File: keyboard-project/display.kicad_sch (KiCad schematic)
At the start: 0 parts

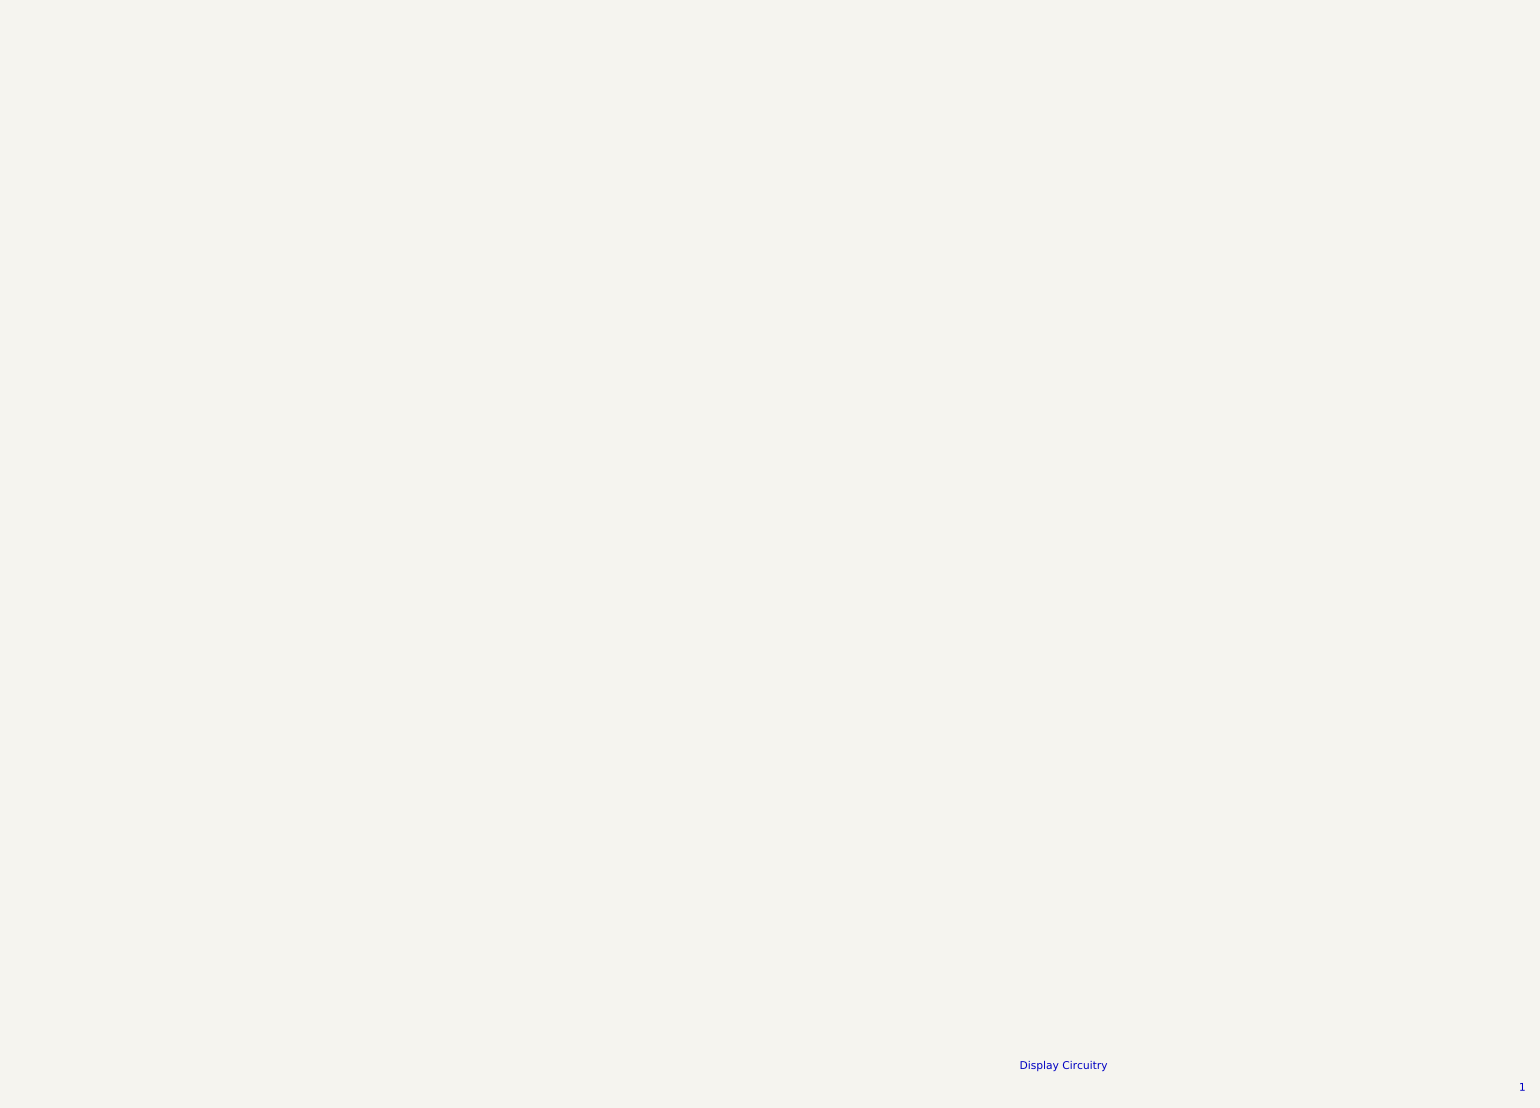
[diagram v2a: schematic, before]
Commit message: encoders, trackball, and display circuits
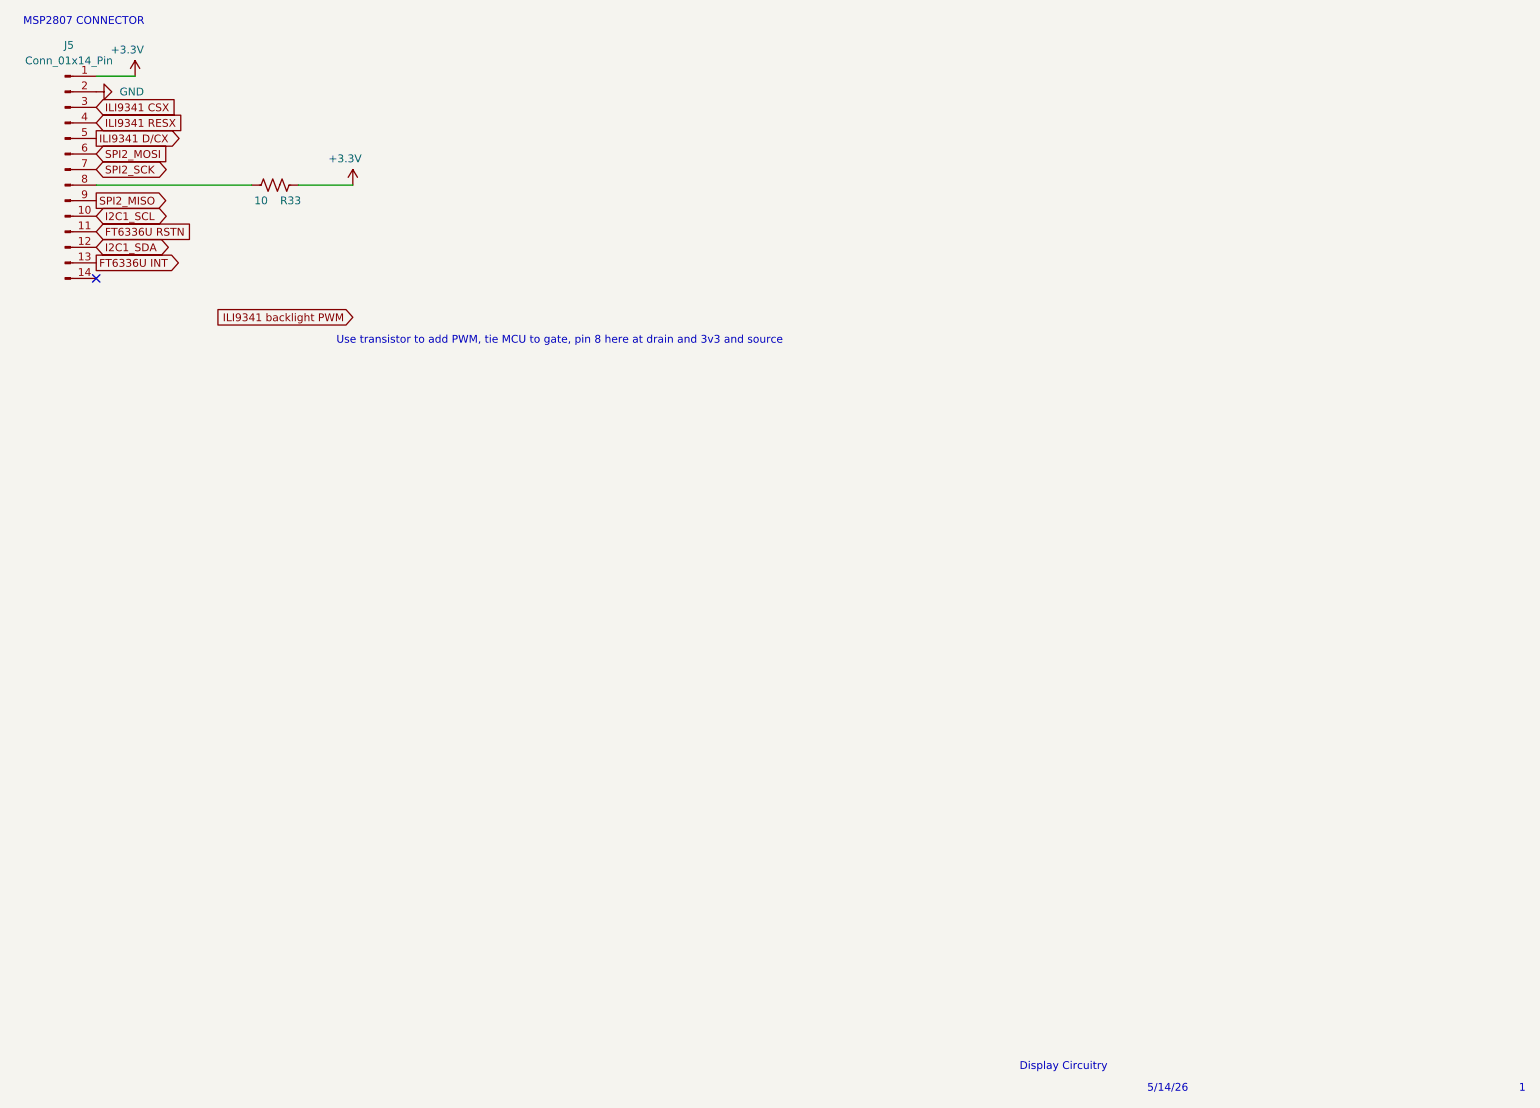
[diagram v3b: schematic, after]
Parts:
- added J5: Conn_01x14_Pin, symbol Connector:Conn_01x14_Pin
- added R33: 10, symbol Device:R_US
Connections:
- new net: J5.8 (Pin_8), R33.1
- new net +3.3V: J5.1 (Pin_1), R33.2
- new net FT6336U INT: J5.13 (Pin_13)
- new net FT6336U RSTN: J5.11 (Pin_11)
- new net GND: J5.2 (Pin_2)
- new net I2C1_SCL: J5.10 (Pin_10)
- new net I2C1_SDA: J5.12 (Pin_12)
- new net ILI9341 CSX: J5.3 (Pin_3)
- new net ILI9341 D/CX: J5.5 (Pin_5)
- new net ILI9341 RESX: J5.4 (Pin_4)
- new net SPI2_MISO: J5.9 (Pin_9)
- new net SPI2_MOSI: J5.6 (Pin_6)
- new net SPI2_SCK: J5.7 (Pin_7)
- no-connect marks 0 -> 1
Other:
- note added: "5/14/26"
- note added: "MSP2807 CONNECTOR"
- note added: "Use transistor to add PWM, tie MCU to gate, pin 8 here at drain and 3v3 and source"

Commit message: res and cap footprints
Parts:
- R33: footprint (none) -> Resistor_SMD:R_1206_3216Metric_Pad1.30x1.75mm_HandSolder
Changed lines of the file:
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@@
 			)
 		)
-		(property "Footprint" ""
+		(property "Footprint" "Resistor_SMD:R_1206_3216Metric_Pad1.30x1.75mm_HandSolder"
 			(at 66.294 44.704 90)
 			(hide yes)

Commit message: more footprints
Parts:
- J5: footprint (none) -> Connector_PinHeader_1.00mm:PinHeader_1x14_P1.00mm_Vertical
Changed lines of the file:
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@@
 			)
 		)
-		(property "Footprint" ""
+		(property "Footprint" "Connector_PinHeader_1.00mm:PinHeader_1x14_P1.00mm_Vertical"
 			(at 31.75 43.18 0)
 			(hide yes)
